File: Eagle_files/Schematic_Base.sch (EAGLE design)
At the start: 30 parts, among them IC1 74LS595N

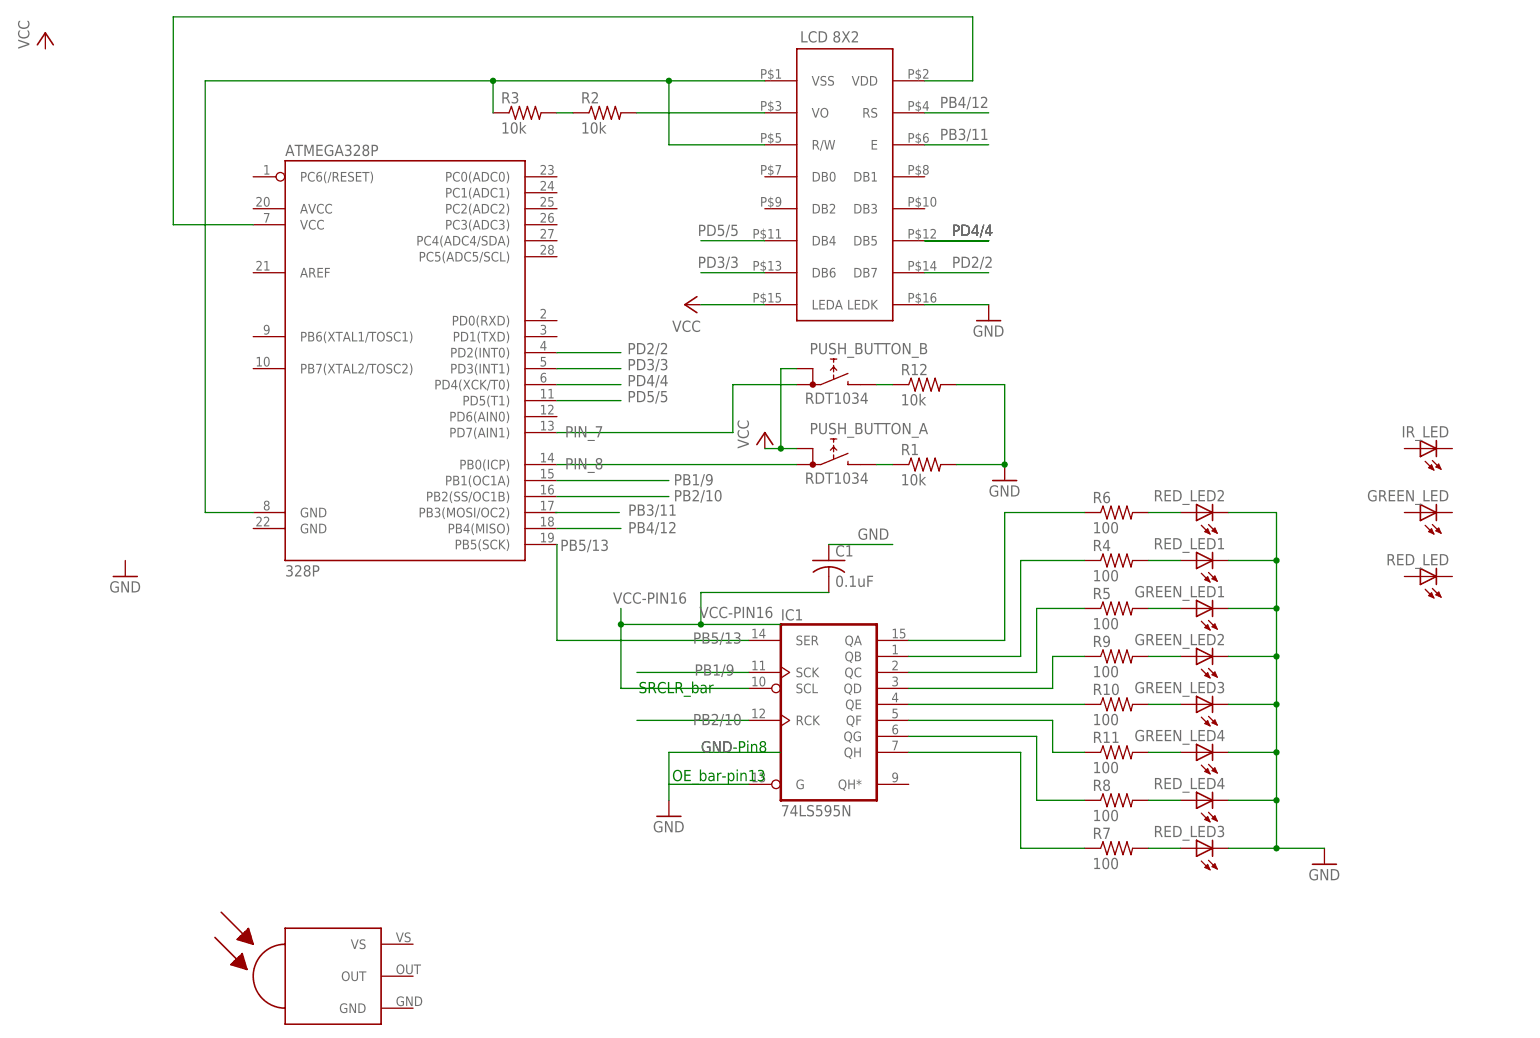
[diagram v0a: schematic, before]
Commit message: Testing ESP8266 on software serial connection
Working.
Tx from Arduino to ESP8266 requires a voltage divider to work.
Able to send and receive on serial port.
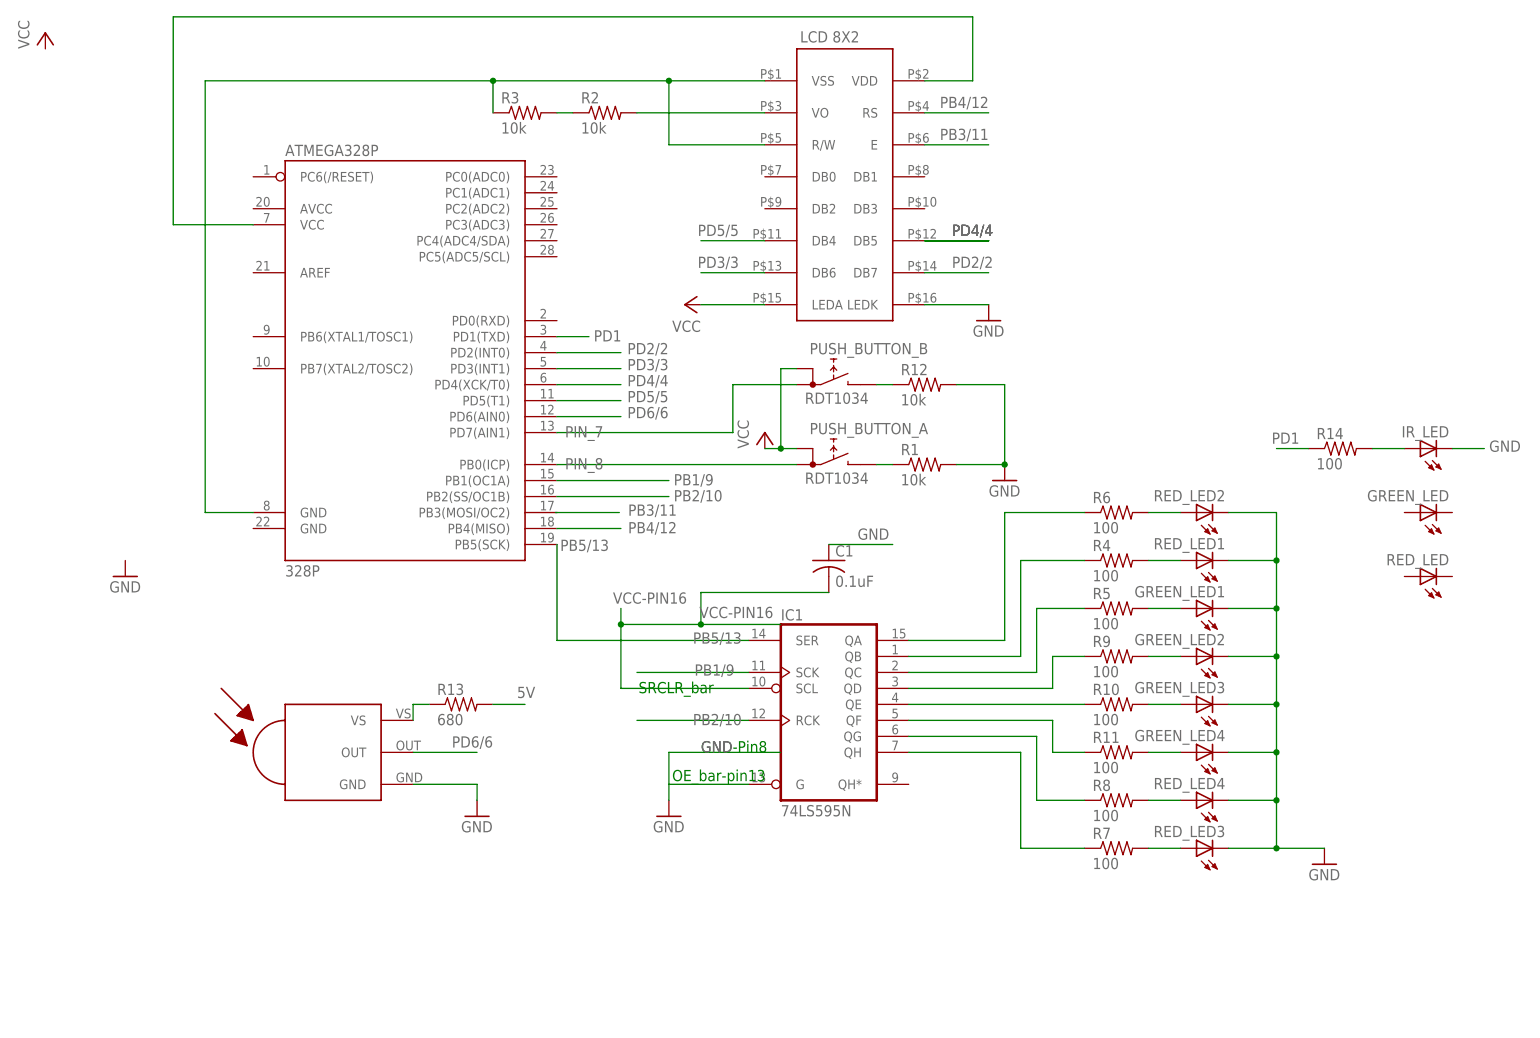
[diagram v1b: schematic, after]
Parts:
- added R13: 680, resistor:R-US_0207/12
- added R14: 100, resistor:R-US_0207/12
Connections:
- new net 5V: R13.2
- new net N$23: R13.1, U$2.VS
- new net N$25: IR_LED.A, R14.2
- new net PD1: R14.1
- new net PD6/6: U$2.OUT
- net GND: now also IR_LED.C, U$2.GND
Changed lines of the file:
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@@
 <part name="PUSH_BUTTON_B" library="switch" library_urn="urn:adsk.eagle:library:380" deviceset="RDT1034" device=""/>
 <part name="R12" library="resistor" library_urn="urn:adsk.eagle:library:348" deviceset="R-US_" device="0207/12" value="10k"/>
+<part name="GND6" library="supply1" library_urn="urn:adsk.eagle:library:371" deviceset="GND" device=""/>
+<part name="R13" library="resistor" library_urn="urn:adsk.eagle:library:348" deviceset="R-US_" device="0207/12" value="680"/>
+<part name="R14" library="resistor" library_urn="urn:adsk.eagle:library:348" deviceset="R-US_" device="0207/12" value="100"/>
 </parts>
 <sheets>
@@
 <instance part="U$1" gate="G$1" x="154.94" y="157.48"/>
 <instance part="IR_LED" gate="G$1" x="246.38" y="114.3" rot="R90"/>
-<instance part="U$2" gate="G$1" x="73.66" y="30.48"/>
+<instance part="U$2" gate="G$1" x="73.66" y="66.04"/>
 <instance part="PUSH_BUTTON_A" gate="G$1" x="152.4" y="114.3"/>
 <instance part="GREEN_LED" gate="G$1" x="246.38" y="104.14" rot="R90"/>
@@
 <instance part="PUSH_BUTTON_B" gate="G$1" x="152.4" y="127"/>
 <instance part="R12" gate="G$1" x="167.64" y="124.46"/>
+<instance part="GND6" gate="1" x="96.52" y="55.88"/>
+<instance part="R13" gate="G$1" x="93.98" y="73.66"/>
+<instance part="R14" gate="G$1" x="233.68" y="114.3"/>
 </instances>
 <busses>
@@
 <pinref part="GND5" gate="1" pin="GND"/>
 </segment>
+<segment>
+<pinref part="U$2" gate="G$1" pin="GND"/>
+<wire x1="86.36" y1="60.96" x2="96.52" y2="60.96" width="0.1524" layer="91"/>
+<wire x1="96.52" y1="60.96" x2="96.52" y2="58.42" width="0.1524" layer="91"/>
+<pinref part="GND6" gate="1" pin="GND"/>
+</segment>
+<segment>
+<pinref part="IR_LED" gate="G$1" pin="C"/>
+<wire x1="251.46" y1="114.3" x2="256.54" y2="114.3" width="0.1524" layer="91"/>
+<label x="257.302" y="113.792" size="1.778" layer="95"/>
+</segment>
 </net>
 <net name="N$3" class="0">
@@
 </segment>
 </net>
+<net name="PD6/6" class="0">
+<segment>
+<pinref part="U$2" gate="G$1" pin="OUT"/>
+<wire x1="86.36" y1="66.04" x2="96.52" y2="66.04" width="0.1524" layer="91"/>
+<label x="99.06" y="68.58" size="1.778" layer="95" rot="R180"/>
+</segment>
+<segment>
+<wire x1="109.22" y1="119.38" x2="119.38" y2="119.38" width="0.1524" layer="91"/>
+<label x="120.396" y="119.126" size="1.778" layer="95"/>
+</segment>
+</net>
+<net name="N$23" class="0">
+<segment>
+<pinref part="R13" gate="G$1" pin="1"/>
+<pinref part="U$2" gate="G$1" pin="VS"/>
+<wire x1="88.9" y1="73.66" x2="86.36" y2="73.66" width="0.1524" layer="91"/>
+<wire x1="86.36" y1="73.66" x2="86.36" y2="71.12" width="0.1524" layer="91"/>
+</segment>
+</net>
+<net name="5V" class="0">
+<segment>
+<pinref part="R13" gate="G$1" pin="2"/>
+<wire x1="99.06" y1="73.66" x2="104.14" y2="73.66" width="0.1524" layer="91"/>
+<label x="102.87" y="74.676" size="1.778" layer="95"/>
+</segment>
+</net>
+<net name="N$25" class="0">
+<segment>
+<pinref part="R14" gate="G$1" pin="2"/>
+<pinref part="IR_LED" gate="G$1" pin="A"/>
+<wire x1="238.76" y1="114.3" x2="243.84" y2="114.3" width="0.1524" layer="91"/>
+</segment>
+</net>
+<net name="PD1" class="0">
+<segment>
+<pinref part="R14" gate="G$1" pin="1"/>
+<wire x1="228.6" y1="114.3" x2="223.52" y2="114.3" width="0.1524" layer="91"/>
+<label x="222.758" y="115.062" size="1.778" layer="95"/>
+</segment>
+<segment>
+<wire x1="114.3" y1="132.08" x2="109.22" y2="132.08" width="0.1524" layer="91"/>
+<label x="115.062" y="131.318" size="1.778" layer="95"/>
+</segment>
+</net>
